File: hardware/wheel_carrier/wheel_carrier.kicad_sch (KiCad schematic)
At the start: 40 parts, among them J1 开发板左排 20P, J10 遥控·前差速, J11 遥控·后差速, J12 BEC 输入 6~7.4V, J13 扩展·左排(直连 J1), J14 扩展·右排(直连 J2), J15 电源排针, J2 开发板右排 20P, J3 霍尔·左前, J4 霍尔·右前, J5 霍尔·左后, J6 霍尔·右后, J7 舵机·前差速, J8 舵机·后差速, J9 遥控·模式, U1 LM2596T-5

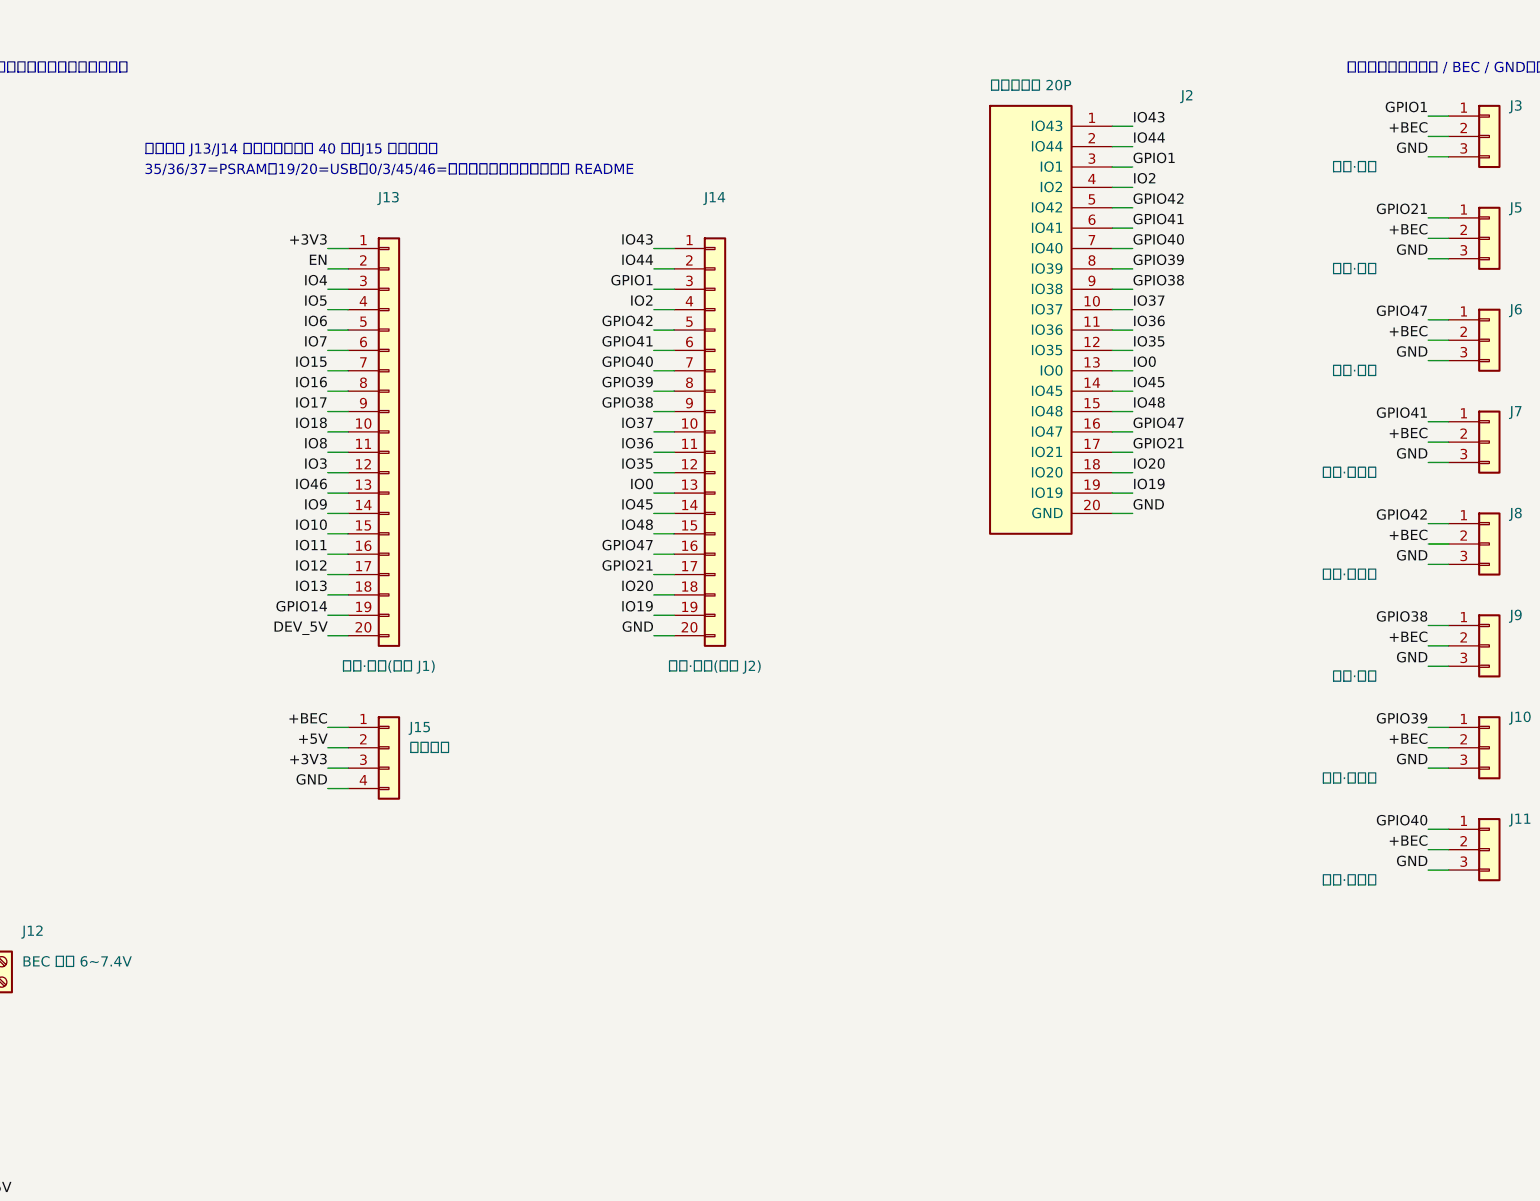
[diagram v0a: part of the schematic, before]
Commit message: feat(hw): v4 改版：2×8 电源条、电调/油门直通口，铺铜缝合与丝印电压标注
- J15 从 1×4 扩成 2×8 电源条（BEC×2 / 5V×3 / 3V3×3，其余 8 针全 GND，
  每列「电源+地」相邻）——一根 2.54 针只插得下一根杜邦线，传感器多了
  原版 4 针不够分；丝印把每个电源脚的电压竖标在所在列正上方，下排两端标 GND
- 新增 J16「电调 BEC 输入」与 J17「接收机·油门」：电调 3 针插头直接进板
  （三针中间必为 +V，插反不反电源），油门信号经板载纯铜直通走线到 J17
  再回接收机——板子不通电也照传；J12 螺丝端子保留，进电只允许一个来源
- 铺铜：J1 上方那条带子（v3 起就被霍尔信号线/焊盘排净空围成孤岛、被
  自动删除）用一根 0.3mm GND 线从第 8/9 针间隙缝回主铺铜，重填后铺满
- gen_pcb 增加 .kicad_pro 自愈：kicad-cli 重写工程文件会丢掉
  lib_footprint_mismatch 的降级忽略（21 条警告复活），每次生成自动补回
- 验证：ERC 0；丝印几何自检 181 条通过；DRC 除已知孤岛提示外零违规；
  预览图与 gerber 包全部重导

Co-Authored-By: Claude Code <noreply@anthropic.com>
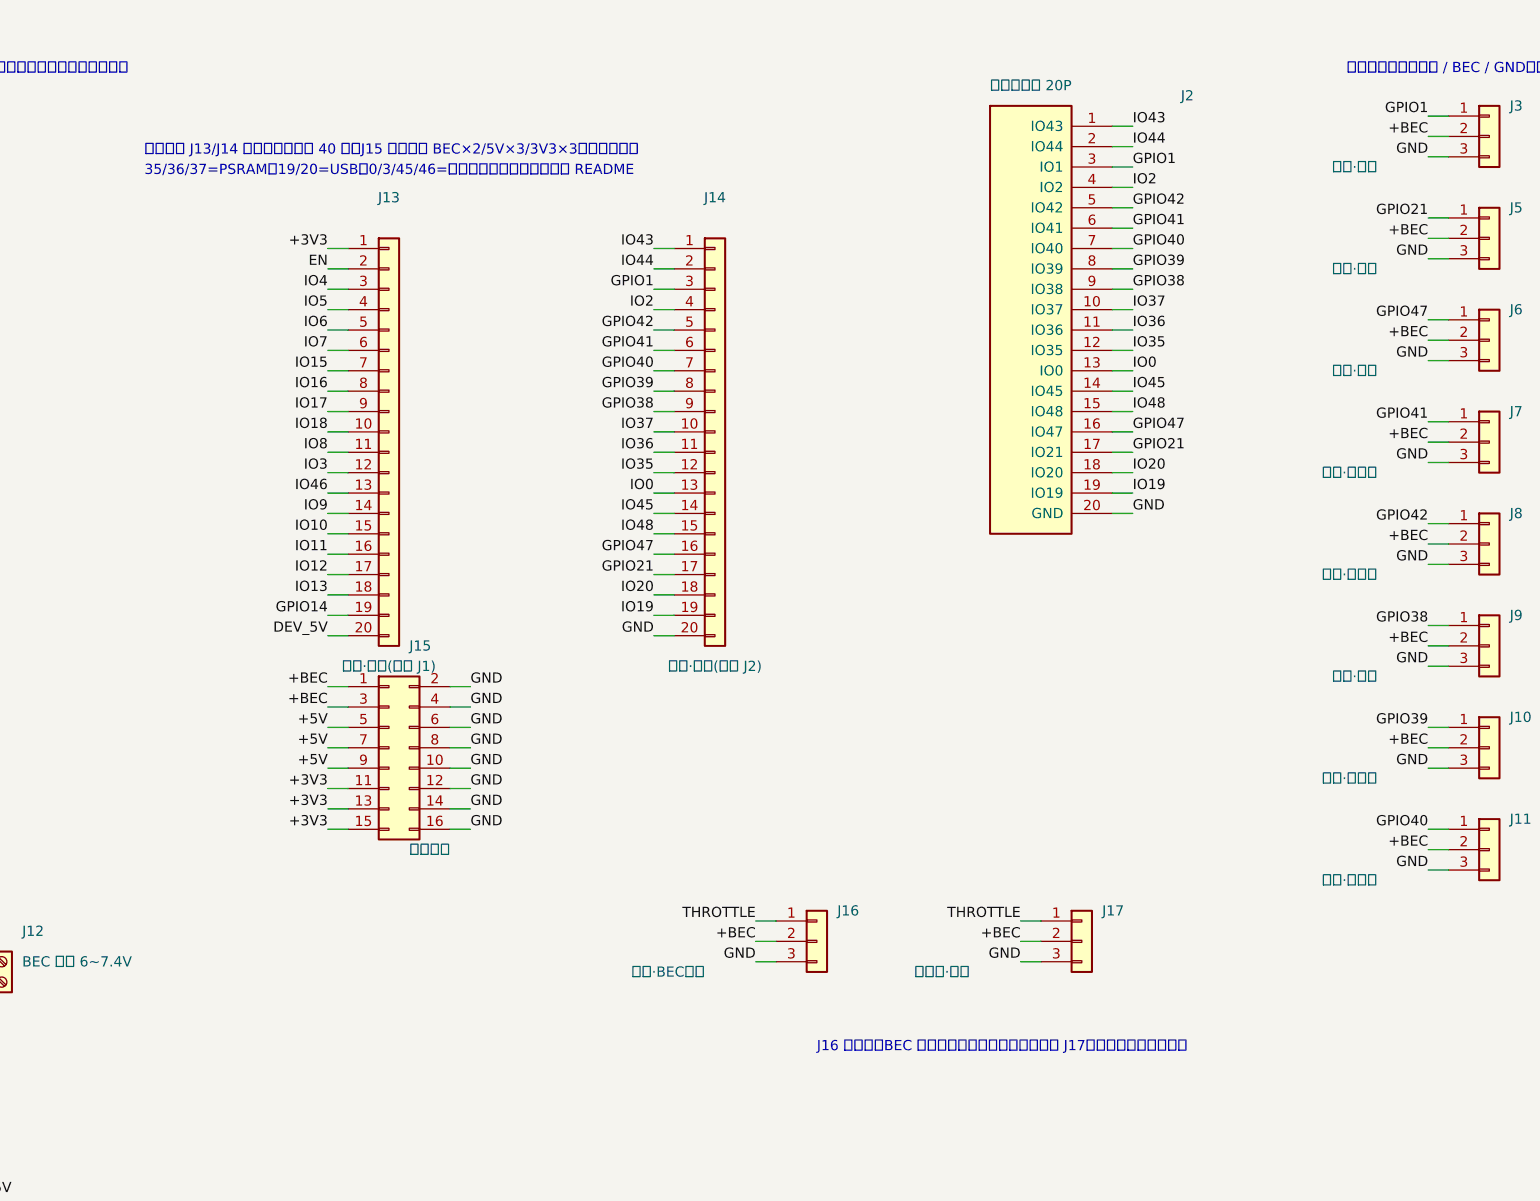
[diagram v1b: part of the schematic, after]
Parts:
- added J16: 电调·BEC输入, Connector_PinHeader_2.54mm:PinHeader_1x03_P2.54mm_Vertical, symbol Connector_Generic:Conn_01x03
- added J17: 接收机·油门, Connector_PinHeader_2.54mm:PinHeader_1x03_P2.54mm_Vertical, symbol Connector_Generic:Conn_01x03
- J15: footprint Connector_PinHeader_2.54mm:PinHeader_1x04_P2.54mm_Vertical -> Connector_PinHeader_2.54mm:PinHeader_2x08_P2.54mm_Vertical; symbol Connector_Generic:Conn_01x04 -> Connector_Generic:Conn_02x08_Odd_Even
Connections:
- net +3V3: now also J15.11 (Pin_11), J15.13 (Pin_13), J15.15 (Pin_15); no longer J15.3 (Pin_3)
- net +5V: now also J15.5 (Pin_5), J15.7 (Pin_7), J15.9 (Pin_9); no longer J15.2 (Pin_2)
- net +BEC: now also J15.3 (Pin_3), J16.2 (Pin_2), J17.2 (Pin_2)
- net GND: now also J15.10 (Pin_10), J15.12 (Pin_12), J15.14 (Pin_14), J15.16 (Pin_16), J15.2 (Pin_2), J15.6 (Pin_6), J15.8 (Pin_8), J16.3 (Pin_3), J17.3 (Pin_3)
- new net THROTTLE: J16.1 (Pin_1), J17.1 (Pin_1)
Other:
- note added: "J16 接电调（BEC 进板）；油门信号经底板直通到 J17，再回接收机油门通道"
- note added: "扩展排针 J13/J14 直连开发板全部 40 针；J15 电源排针 BEC×2/5V×3/3V3×3，其余全是地"
- note removed: "扩展排针 J13/J14 直连开发板全部 40 针；J15 是电源排针"

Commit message: feat(hw): 4S 输入升级 C1/R5/D3，补使用说明书
J12 端子可接 4S（≤16.8V）：C1 1000µF/25V、R5 1.5k、D3 SB560；原理图/PCB 器件值同步，封装和铜箔不变，接收机 +BEC 脚保持原样。

4S 时靠接线手动断开接收机/舵机 +V；README BOM 同步，新增 hardware/使用说明书.md。

Co-Authored-By: Claude Code <noreply@anthropic.com>
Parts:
- C1: value 1000µF/16V -> 1000µF/25V
- D3: value 1N5822 -> SB560
- R5: value 1k -> 1.5k
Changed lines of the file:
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@@
       (effects (font (size 1.27 1.27)) (justify left))
     )
-    (property "Value" "1000µF/16V"
+    (property "Value" "1000µF/25V"
       (at 133.35 204.47 0)
       (effects (font (size 1.27 1.27)) (justify left))
@@
       (effects (font (size 1.27 1.27)))
     )
-    (property "Value" "1N5822"
+    (property "Value" "SB560"
       (at 146.05 240.03 90)
       (effects (font (size 1.27 1.27)))
@@
       (effects (font (size 1.27 1.27)) (justify left))
     )
-    (property "Value" "1k"
+    (property "Value" "1.5k"
       (at 127 205.74 0)
       (effects (font (size 1.27 1.27)) (justify left))

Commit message: feat(hw): v6 正面插装、舵机 5V、A3144 脚序，遥控三通道合并
- 开发板改为正面插装：J1 接右排 IO43 列，J2 接左排 3V3 列，针 1 仍在左端
- J7/J8 舵机 +V 改接板载 5V；J17 保持 BEC，接收机电源/地仍走 J17
- 霍尔 J3~J6 改为 +V/GND/信号，匹配 A3144 1=VCC、2=GND、3=OUT
- J10/J11 取消，遥控三通道合并为 J9 三针信号排针
- C4 升级 1000µF/16V，加强 5V 舵机瞬态
- 同步丝印、走线、脚序断言、README 与使用说明书；ERC/DRC 均 0/0

Co-Authored-By: Claude Code <noreply@anthropic.com>
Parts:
- removed J10: 遥控·前差速, Connector_PinHeader_2.54mm:PinHeader_1x03_P2.54mm_Vertical, symbol Connector_Generic:Conn_01x03
- removed J11: 遥控·后差速, Connector_PinHeader_2.54mm:PinHeader_1x03_P2.54mm_Vertical, symbol Connector_Generic:Conn_01x03
- C4: value 220µF/16V -> 1000µF/16V
- J1: value 开发板左排 20P -> 开发板排母1·右排 IO43 列; symbol wheel_carrier:DevBoard_Row_L -> wheel_carrier:DevBoard_Row_R
- J13: value 扩展·左排(直连 J1) -> 扩展·排母1(直连 J1/右排)
- J14: value 扩展·右排(直连 J2) -> 扩展·排母2(直连 J2/左排)
- J2: value 开发板右排 20P -> 开发板排母2·左排 3V3 列; symbol wheel_carrier:DevBoard_Row_R -> wheel_carrier:DevBoard_Row_L
- J9: value 遥控·模式 -> 遥控·三通道信号
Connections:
- net +3V3: now also J14.1 (Pin_1), J2.1 (3V3); no longer J1.1 (3V3), J13.1 (Pin_1)
- net +5V: now also J7.2 (Pin_2), J8.2 (Pin_2)
- net +BEC: now also J3.1 (Pin_1), J4.1 (Pin_1), J5.1 (Pin_1), J6.1 (Pin_1); no longer J3.2 (Pin_2), J4.2 (Pin_2), J5.2 (Pin_2), J6.2 (Pin_2), J7.2 (Pin_2), J8.2 (Pin_2), J9.2 (Pin_2)
- net DEV_5V: now also J14.20 (Pin_20), J2.20 (5V); no longer J1.20 (5V), J13.20 (Pin_20)
- net EN: now also J14.2 (Pin_2), J2.2 (EN); no longer J1.2 (EN), J13.2 (Pin_2)
- net GND: now also J1.20 (GND), J13.20 (Pin_20), J3.2 (Pin_2), J4.2 (Pin_2), J5.2 (Pin_2), J6.2 (Pin_2); no longer J14.20 (Pin_20), J2.20 (GND), J3.3 (Pin_3), J4.3 (Pin_3), J5.3 (Pin_3), J6.3 (Pin_3), J9.3 (Pin_3)
- net GPIO1: now also J1.3 (IO1), J13.3 (Pin_3), J3.3 (Pin_3); no longer J14.3 (Pin_3), J2.3 (IO1), J3.1 (Pin_1)
- net GPIO14: now also J14.19 (Pin_19), J2.19 (IO14), J4.3 (Pin_3); no longer J1.19 (IO14), J13.19 (Pin_19), J4.1 (Pin_1)
- net GPIO21: now also J1.17 (IO21), J13.17 (Pin_17), J5.3 (Pin_3); no longer J14.17 (Pin_17), J2.17 (IO21), J5.1 (Pin_1)
- net GPIO38: now also J1.9 (IO38), J13.9 (Pin_9); no longer J14.9 (Pin_9), J2.9 (IO38)
- net GPIO39: now also J1.8 (IO39), J13.8 (Pin_8), J9.2 (Pin_2); no longer J14.8 (Pin_8), J2.8 (IO39)
- net GPIO40: now also J1.7 (IO40), J13.7 (Pin_7), J9.3 (Pin_3); no longer J14.7 (Pin_7), J2.7 (IO40)
- net GPIO41: now also J1.6 (IO41), J13.6 (Pin_6); no longer J14.6 (Pin_6), J2.6 (IO41)
- net GPIO42: now also J1.5 (IO42), J13.5 (Pin_5); no longer J14.5 (Pin_5), J2.5 (IO42)
- net GPIO47: now also J1.16 (IO47), J13.16 (Pin_16), J6.3 (Pin_3); no longer J14.16 (Pin_16), J2.16 (IO47), J6.1 (Pin_1)
- net IO0: now also J1.13 (IO0), J13.13 (Pin_13); no longer J14.13 (Pin_13), J2.13 (IO0)
- net IO10: now also J14.15 (Pin_15), J2.15 (IO10); no longer J1.15 (IO10), J13.15 (Pin_15)
- net IO11: now also J14.16 (Pin_16), J2.16 (IO11); no longer J1.16 (IO11), J13.16 (Pin_16)
- net IO12: now also J14.17 (Pin_17), J2.17 (IO12); no longer J1.17 (IO12), J13.17 (Pin_17)
- net IO13: now also J14.18 (Pin_18), J2.18 (IO13); no longer J1.18 (IO13), J13.18 (Pin_18)
- net IO15: now also J14.7 (Pin_7), J2.7 (IO15); no longer J1.7 (IO15), J13.7 (Pin_7)
- net IO16: now also J14.8 (Pin_8), J2.8 (IO16); no longer J1.8 (IO16), J13.8 (Pin_8)
- net IO17: now also J14.9 (Pin_9), J2.9 (IO17); no longer J1.9 (IO17), J13.9 (Pin_9)
- net IO18: now also J14.10 (Pin_10), J2.10 (IO18); no longer J1.10 (IO18), J13.10 (Pin_10)
- net IO19: now also J1.19 (IO19), J13.19 (Pin_19); no longer J14.19 (Pin_19), J2.19 (IO19)
- net IO2: now also J1.4 (IO2), J13.4 (Pin_4); no longer J14.4 (Pin_4), J2.4 (IO2)
- net IO20: now also J1.18 (IO20), J13.18 (Pin_18); no longer J14.18 (Pin_18), J2.18 (IO20)
- net IO3: now also J14.12 (Pin_12), J2.12 (IO3); no longer J1.12 (IO3), J13.12 (Pin_12)
- net IO35: now also J1.12 (IO35), J13.12 (Pin_12); no longer J14.12 (Pin_12), J2.12 (IO35)
- net IO36: now also J1.11 (IO36), J13.11 (Pin_11); no longer J14.11 (Pin_11), J2.11 (IO36)
- net IO37: now also J1.10 (IO37), J13.10 (Pin_10); no longer J14.10 (Pin_10), J2.10 (IO37)
- net IO4: now also J14.3 (Pin_3), J2.3 (IO4); no longer J1.3 (IO4), J13.3 (Pin_3)
- net IO43: now also J1.1 (IO43), J13.1 (Pin_1); no longer J14.1 (Pin_1), J2.1 (IO43)
- net IO44: now also J1.2 (IO44), J13.2 (Pin_2); no longer J14.2 (Pin_2), J2.2 (IO44)
- net IO45: now also J1.14 (IO45), J13.14 (Pin_14); no longer J14.14 (Pin_14), J2.14 (IO45)
- net IO46: now also J14.13 (Pin_13), J2.13 (IO46); no longer J1.13 (IO46), J13.13 (Pin_13)
- net IO48: now also J1.15 (IO48), J13.15 (Pin_15); no longer J14.15 (Pin_15), J2.15 (IO48)
- net IO5: now also J14.4 (Pin_4), J2.4 (IO5); no longer J1.4 (IO5), J13.4 (Pin_4)
- net IO6: now also J14.5 (Pin_5), J2.5 (IO6); no longer J1.5 (IO6), J13.5 (Pin_5)
- net IO7: now also J14.6 (Pin_6), J2.6 (IO7); no longer J1.6 (IO7), J13.6 (Pin_6)
- net IO8: now also J14.11 (Pin_11), J2.11 (IO8); no longer J1.11 (IO8), J13.11 (Pin_11)
- net IO9: now also J14.14 (Pin_14), J2.14 (IO9); no longer J1.14 (IO9), J13.14 (Pin_14)
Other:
- note added: "BEC 输入 6~7.4V：板上降到 5V 给开发板和舵机；霍尔、J16/J17 走 BEC 原电压"
- note added: "J16 接电调（BEC 进板）；油门信号经底板直通到 J17，再回接收机油门通道；J17 给接收机供电"
- note added: "扩展排针 J13/J14 直连开发板全部 40 针（J13=J1、J14=J2）；J15 电源排针 BEC×2/5V×3/3V3×3"
- note added: "正面插装：J1 对开发板右排 IO43 列，J2 对左排 3V3 列；针号 1 在远离 USB 的一端"
- note added: "舵机：信号/5V/GND；霍尔：+V/GND/信号（A3144）；遥控 J9：三路信号，无电源/地"
- note removed: "BEC 输入 6~7.4V：板上降到 5V 给开发板；舵机/接收机/霍尔走 BEC 原电压"
- note removed: "J16 接电调（BEC 进板）；油门信号经底板直通到 J17，再回接收机油门通道"
- note removed: "扩展排针 J13/J14 直连开发板全部 40 针；J15 电源排针 BEC×2/5V×3/3V3×3，其余全是地"
- note removed: "接口顺序统一：信号 / BEC / GND，与舵机、接收机插头一致"
- note removed: "针号 1 从开发板远离 USB 口的一端数起；装板前对开发板丝印核一遍"
- moved on the sheet: J1, J2
